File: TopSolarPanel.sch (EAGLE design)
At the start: 18 parts

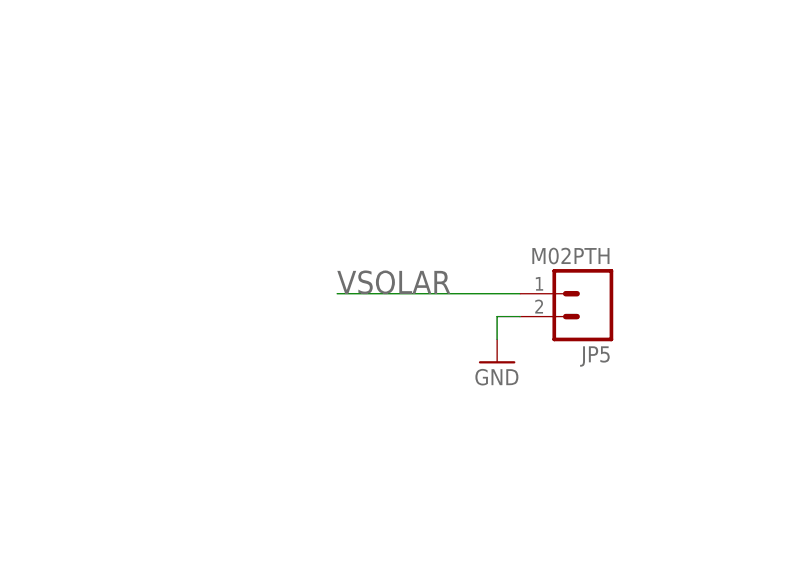
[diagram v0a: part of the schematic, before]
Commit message: Fixed solar cell footprints
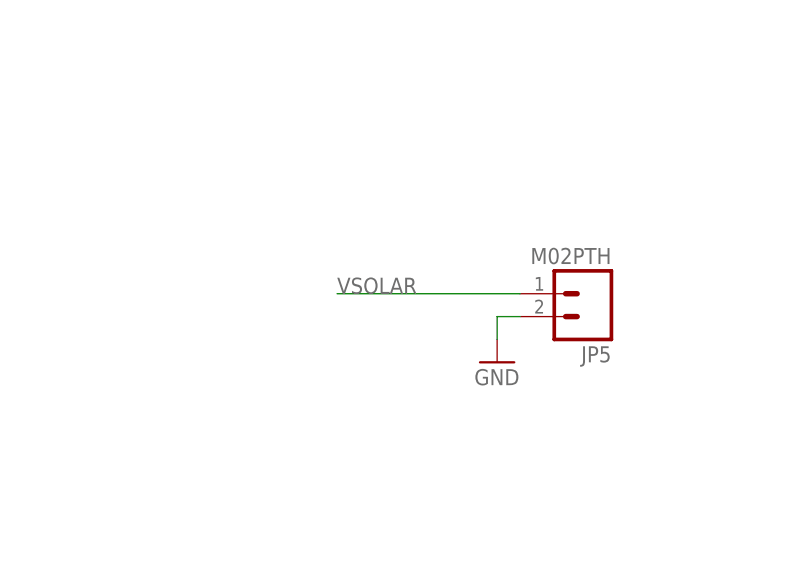
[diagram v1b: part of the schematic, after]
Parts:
- D1, D2, D3, D4, D5, D6: device phonesat:SB_DIODE -> Solar:SB_DIODE
- SL1, SL10, SL2, SL3, SL4, SL5, SL6, SL7, SL8, SL9: device phonesat:SOLAR_CELL -> Solar:SOLAR_CELL
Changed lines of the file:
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@@
 </classes>
 <parts>
-<part name="SL3" library="phonesat" deviceset="SOLAR_CELL" device=""/>
-<part name="D2" library="phonesat" deviceset="SB_DIODE" device=""/>
-<part name="SL5" library="phonesat" deviceset="SOLAR_CELL" device=""/>
-<part name="SL1" library="phonesat" deviceset="SOLAR_CELL" device=""/>
-<part name="SL7" library="phonesat" deviceset="SOLAR_CELL" device=""/>
-<part name="SL10" library="phonesat" deviceset="SOLAR_CELL" device=""/>
-<part name="SL6" library="phonesat" deviceset="SOLAR_CELL" device=""/>
-<part name="SL4" library="phonesat" deviceset="SOLAR_CELL" device=""/>
-<part name="SL8" library="phonesat" deviceset="SOLAR_CELL" device=""/>
-<part name="SL9" library="phonesat" deviceset="SOLAR_CELL" device=""/>
-<part name="SL2" library="phonesat" deviceset="SOLAR_CELL" device=""/>
-<part name="D1" library="phonesat" deviceset="SB_DIODE" device=""/>
-<part name="D3" library="phonesat" deviceset="SB_DIODE" device=""/>
-<part name="D4" library="phonesat" deviceset="SB_DIODE" device=""/>
-<part name="D5" library="phonesat" deviceset="SB_DIODE" device=""/>
-<part name="D6" library="phonesat" deviceset="SB_DIODE" device=""/>
+<part name="SL3" library="Solar" deviceset="SOLAR_CELL" device=""/>
+<part name="D2" library="Solar" deviceset="SB_DIODE" device=""/>
+<part name="SL5" library="Solar" deviceset="SOLAR_CELL" device=""/>
+<part name="SL1" library="Solar" deviceset="SOLAR_CELL" device=""/>
+<part name="SL7" library="Solar" deviceset="SOLAR_CELL" device=""/>
+<part name="SL10" library="Solar" deviceset="SOLAR_CELL" device=""/>
+<part name="SL6" library="Solar" deviceset="SOLAR_CELL" device=""/>
+<part name="SL4" library="Solar" deviceset="SOLAR_CELL" device=""/>
+<part name="SL8" library="Solar" deviceset="SOLAR_CELL" device=""/>
+<part name="SL9" library="Solar" deviceset="SOLAR_CELL" device=""/>
+<part name="SL2" library="Solar" deviceset="SOLAR_CELL" device=""/>
+<part name="D1" library="Solar" deviceset="SB_DIODE" device=""/>
+<part name="D3" library="Solar" deviceset="SB_DIODE" device=""/>
+<part name="D4" library="Solar" deviceset="SB_DIODE" device=""/>
+<part name="D5" library="Solar" deviceset="SB_DIODE" device=""/>
+<part name="D6" library="Solar" deviceset="SB_DIODE" device=""/>
 <part name="GND1" library="SparkFun" deviceset="GND" device=""/>
 <part name="FRAME1" library="SparkFun-Aesthetics" deviceset="FRAME-LETTER" device=""/>
@@
 <pinref part="JP5" gate="G$1" pin="1"/>
 <wire x1="198.12" y1="111.76" x2="177.8" y2="111.76" width="0.1524" layer="91"/>
-<label x="177.8" y="111.76" size="2.54" layer="95"/>
+<label x="177.8" y="111.76" size="1.778" layer="95"/>
 </segment>
 </net>

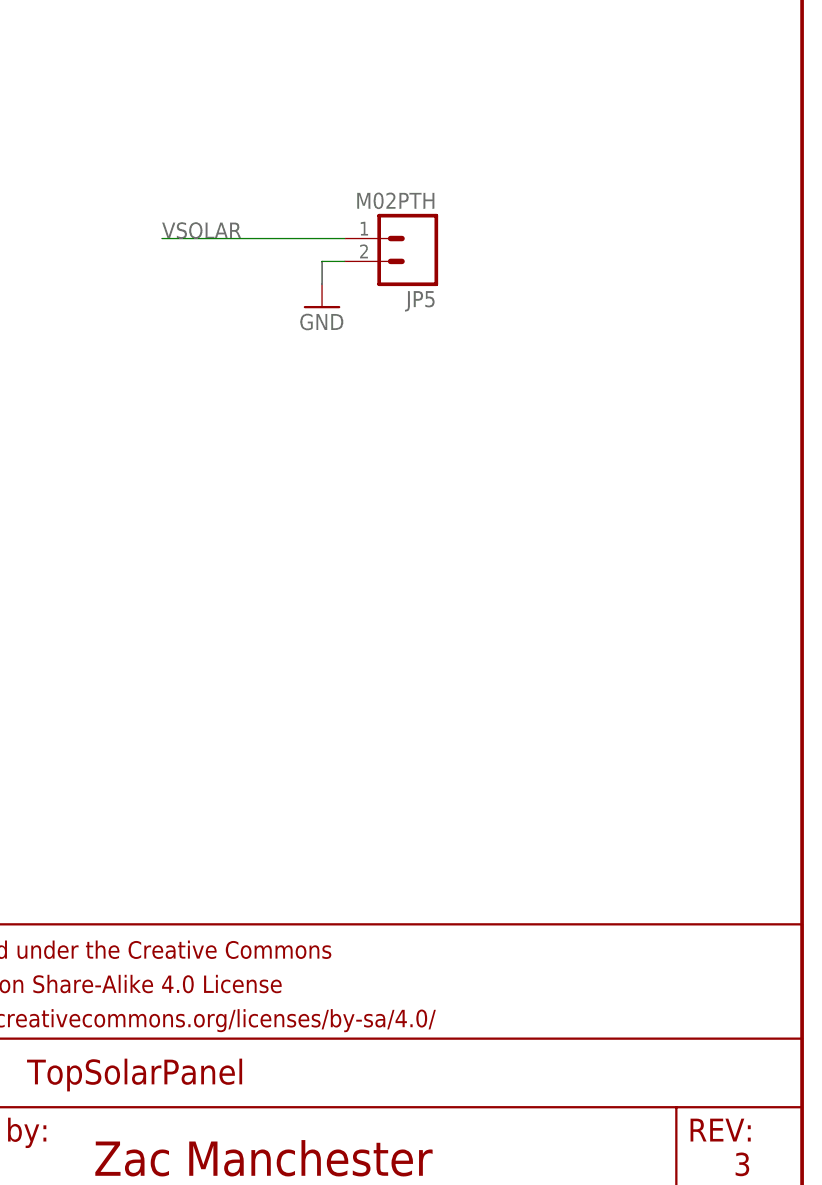
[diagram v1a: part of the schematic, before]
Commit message: New top solar panel
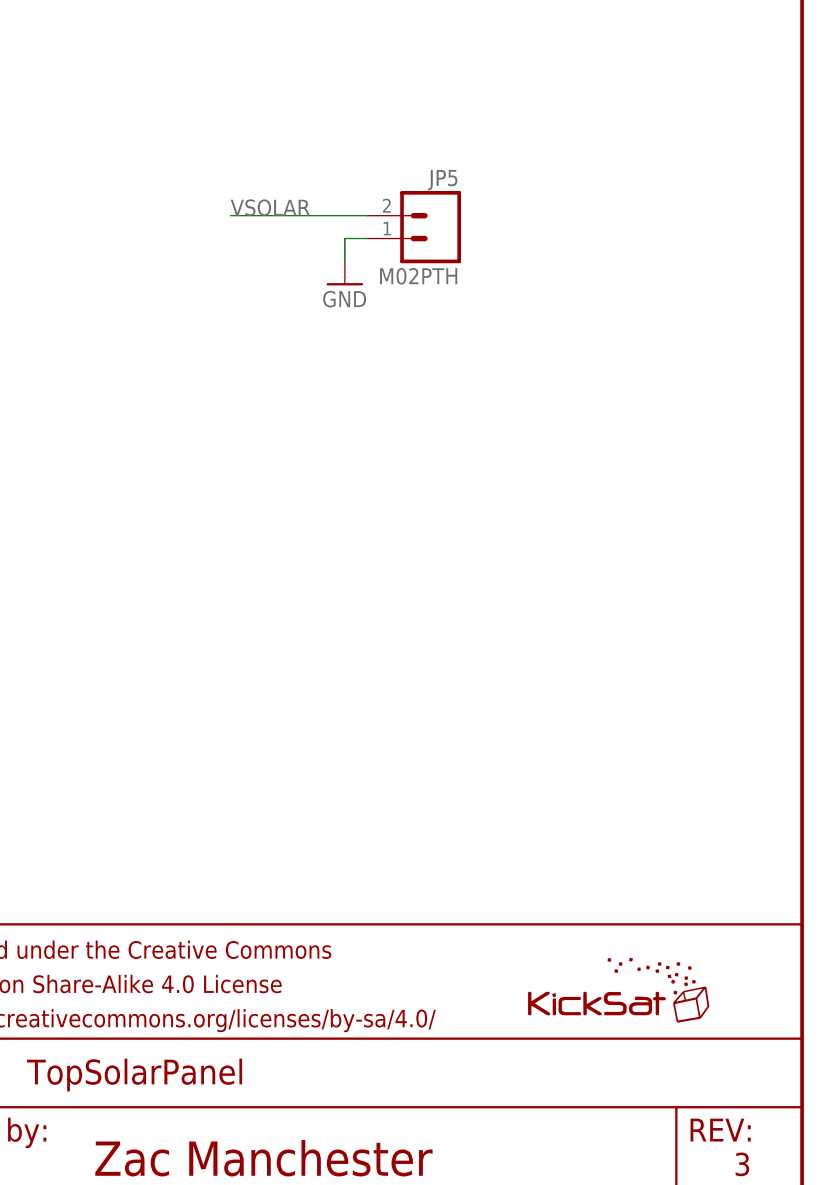
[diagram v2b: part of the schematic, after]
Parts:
- added U$1: KICKSAT_LOGO, KickSat-Logo:KICKSAT_LOGO
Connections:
- net GND: now also JP5.1; no longer JP5.2
- net VSOLAR: now also JP5.2; no longer JP5.1
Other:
- moved on the sheet: JP5
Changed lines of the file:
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@@
 <part name="JP5" library="SparkFun-Connectors" deviceset="M02" device="PTH"/>
 <part name="GND2" library="SparkFun" deviceset="GND" device=""/>
+<part name="U$1" library="KickSat-Logo" deviceset="KICKSAT_LOGO" device=""/>
 </parts>
 <sheets>
@@
 <instance part="FRAME1" gate="G$1" x="0" y="0"/>
 <instance part="FRAME1" gate="G$2" x="147.32" y="0"/>
-<instance part="JP5" gate="G$1" x="205.74" y="111.76" rot="R180"/>
-<instance part="GND2" gate="1" x="195.58" y="104.14"/>
+<instance part="JP5" gate="G$1" x="208.28" y="111.76" rot="MR0"/>
+<instance part="GND2" gate="1" x="198.12" y="106.68"/>
+<instance part="U$1" gate="G$1" x="218.44" y="25.4"/>
 </instances>
 <busses>
@@
 </segment>
 <segment>
-<pinref part="JP5" gate="G$1" pin="1"/>
-<wire x1="198.12" y1="111.76" x2="177.8" y2="111.76" width="0.1524" layer="91"/>
-<label x="177.8" y="111.76" size="1.778" layer="95"/>
+<pinref part="JP5" gate="G$1" pin="2"/>
+<wire x1="200.66" y1="114.3" x2="185.42" y2="114.3" width="0.1524" layer="91"/>
+<label x="185.42" y="114.3" size="1.778" layer="95"/>
 </segment>
 </net>
@@
 </segment>
 <segment>
-<pinref part="JP5" gate="G$1" pin="2"/>
-<wire x1="198.12" y1="109.22" x2="195.58" y2="109.22" width="0.1524" layer="91"/>
-<wire x1="195.58" y1="109.22" x2="195.58" y2="106.68" width="0.1524" layer="91"/>
+<pinref part="JP5" gate="G$1" pin="1"/>
 <pinref part="GND2" gate="1" pin="GND"/>
+<wire x1="200.66" y1="111.76" x2="198.12" y2="111.76" width="0.1524" layer="91"/>
+<wire x1="198.12" y1="111.76" x2="198.12" y2="109.22" width="0.1524" layer="91"/>
 </segment>
 </net>
